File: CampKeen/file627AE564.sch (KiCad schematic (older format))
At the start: 16 parts, among them Q16 2N7000, Q17 2N7000, Q18 2N7000, Q19 2N7000

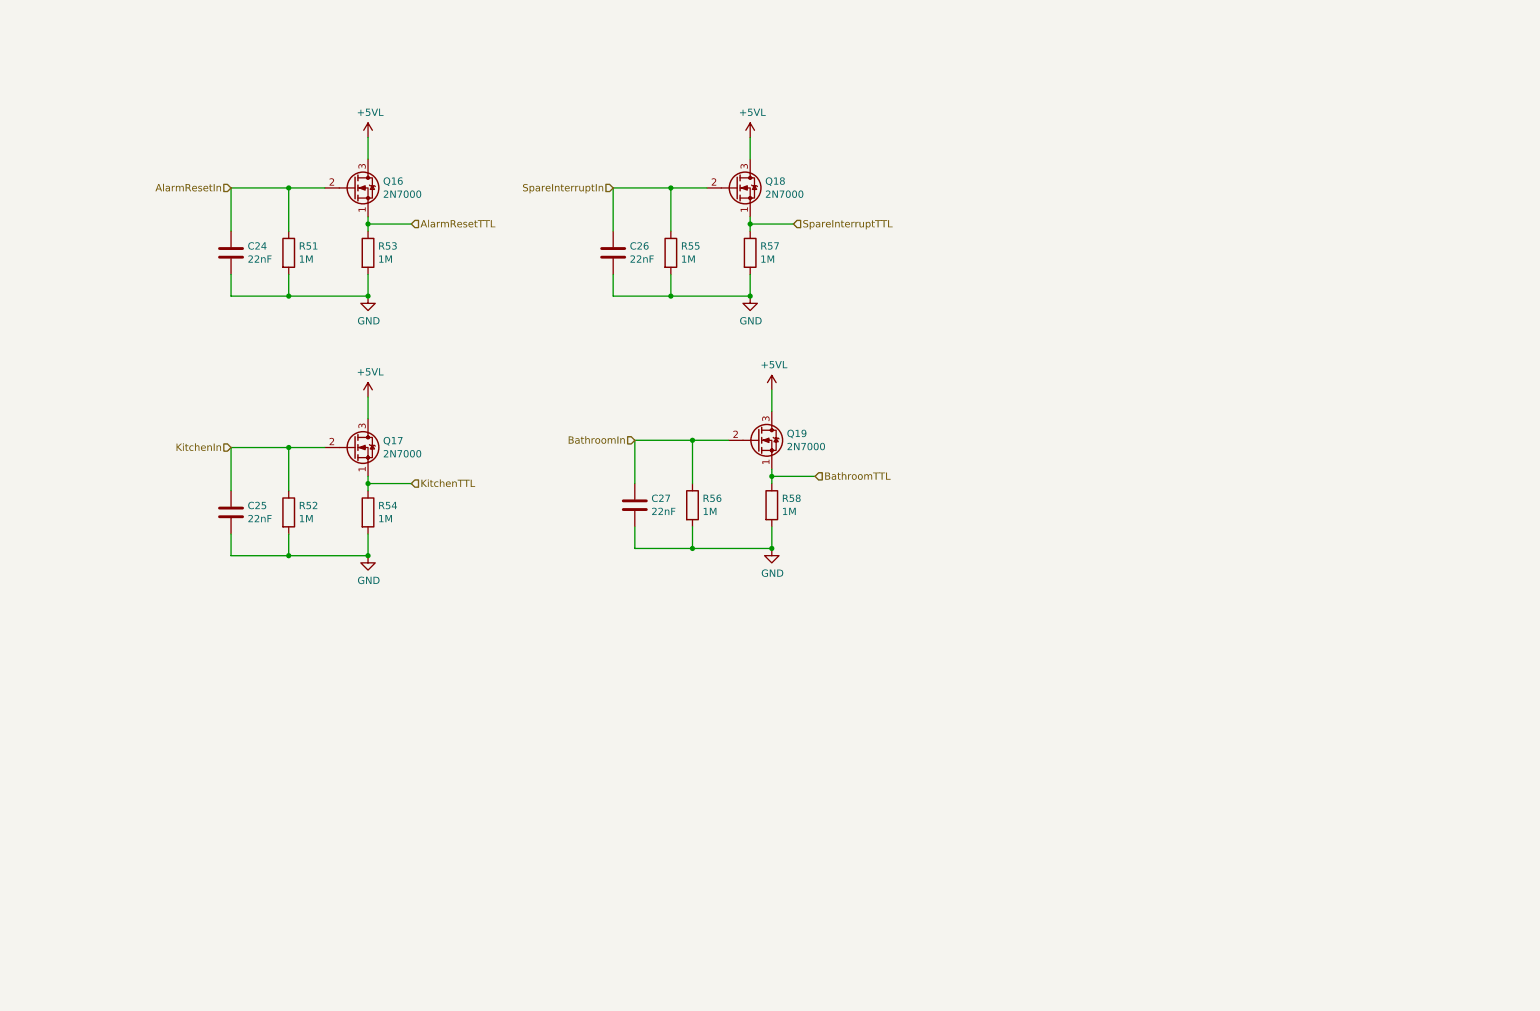
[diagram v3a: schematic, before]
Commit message: wip for working on the input circuits on the board. they are getting upgraded with opto-isolation as i've found that you can burn out the processor board if there is a voltage applied to an input when the system is on and then turned off. for the code fixing some of the LCD display code.
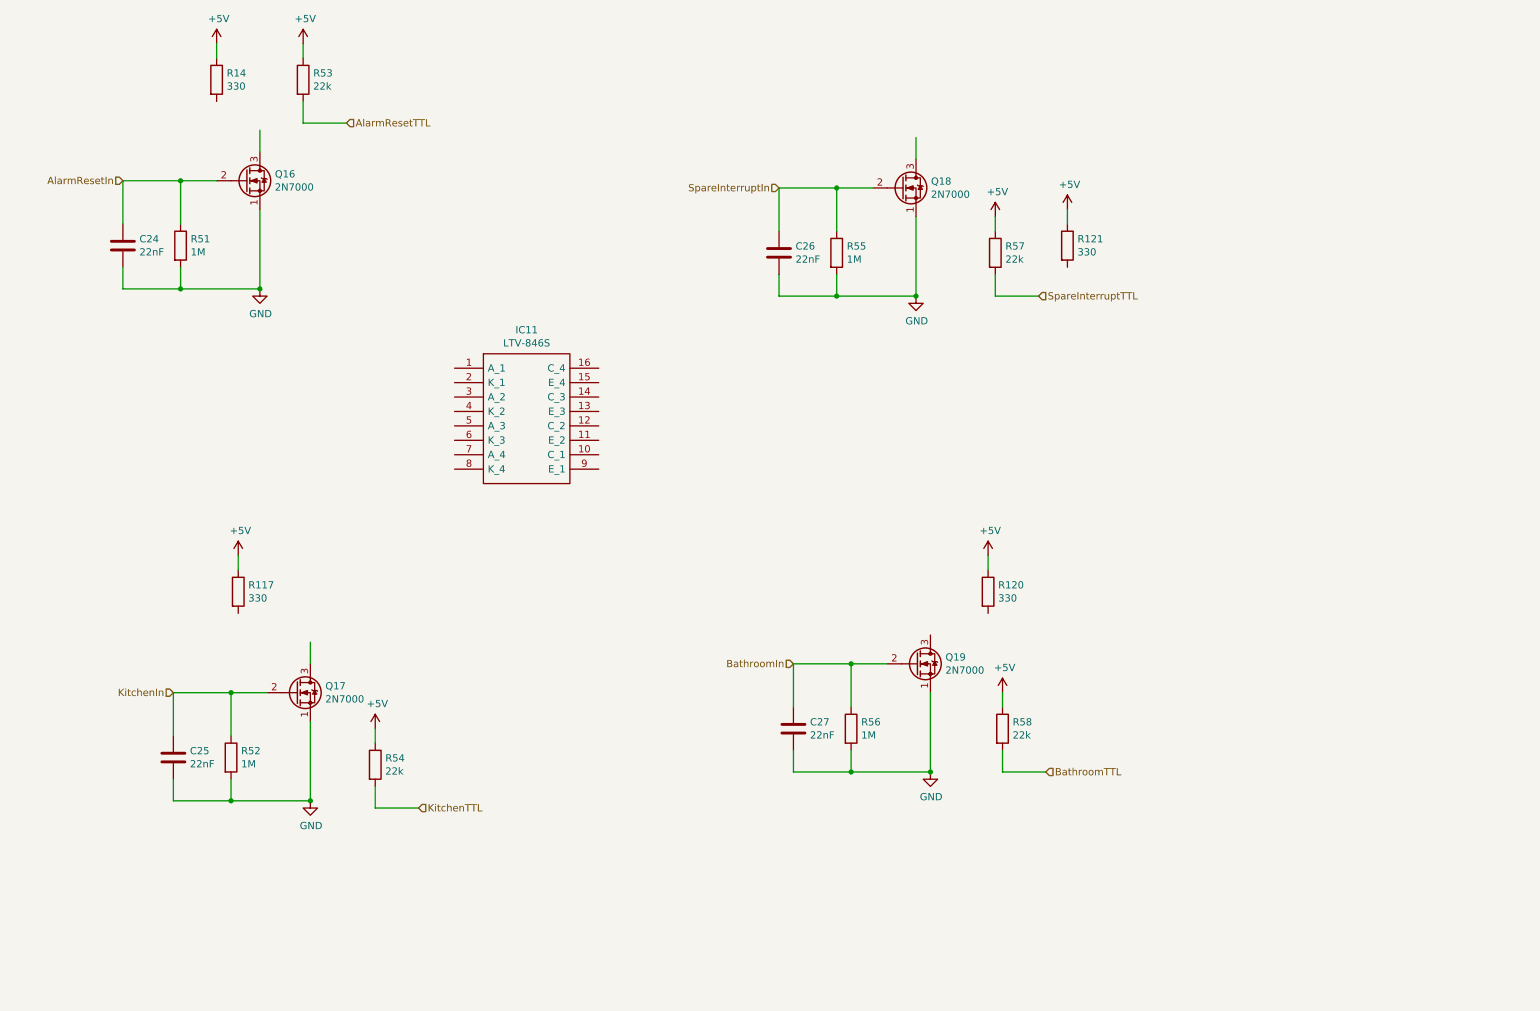
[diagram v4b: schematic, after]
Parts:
- added IC11: LTV-846S, SOP254P1016X460-16N, symbol SamacSys_Parts:LTV-846S
- added R117, R120, R121, R14: 330, Resistor_THT:R_Axial_DIN0207_L6.3mm_D2.5mm_P2.54mm_Vertical, symbol Device:R
- R53, R54, R57, R58: value 1M -> 22k
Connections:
- net labels added: +5V
- net labels removed: +5VL
- wire segments 52 -> 55
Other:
- moved on the sheet: C24, C25, C26, C27, Q16, Q17, Q18, Q19, R51, R52, R53, R54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

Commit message: schematic done for Input isolation updates.
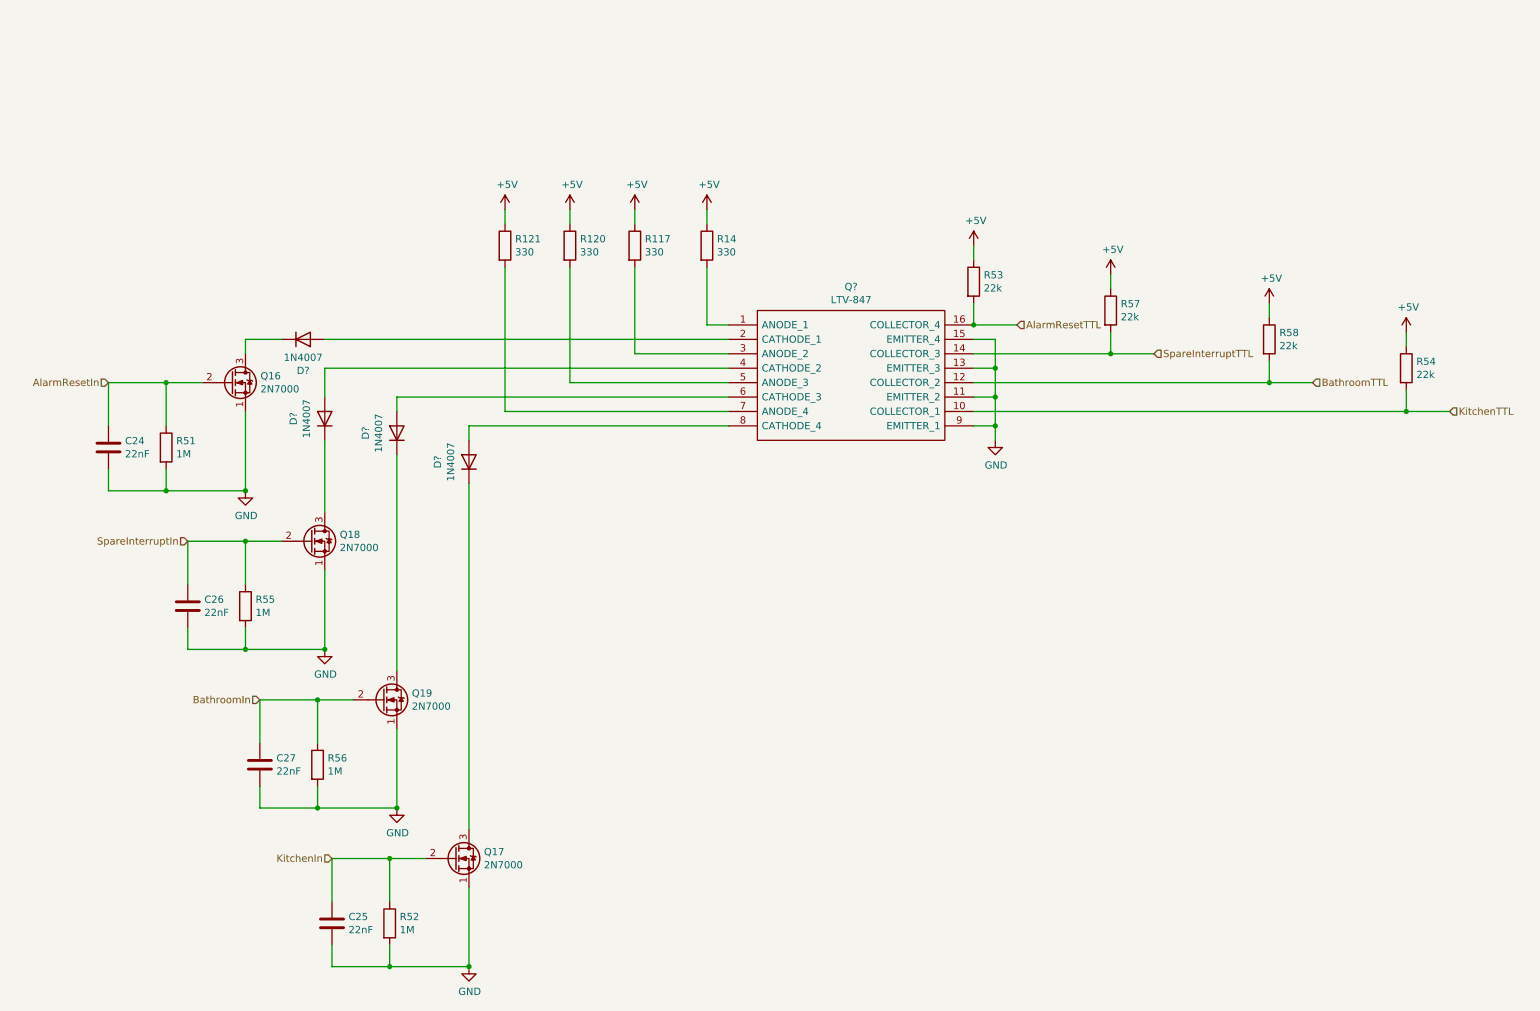
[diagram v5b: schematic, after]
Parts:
- removed IC11: LTV-846S, SOP254P1016X460-16N, symbol SamacSys_Parts:LTV-846S
- added D? (x4): 1N4007, Diode_THT:D_DO-41_SOD81_P10.16mm_Horizontal, symbol Diode:1N4007
- added Q?: LTV-847, DIP762W60P254L1984H450Q16N, symbol SamacSys_Parts:LTV-847
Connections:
- wire segments 55 -> 83
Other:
- moved on the sheet: C24, C25, C26, C27, Q16, Q17, Q18, Q19, R117, R120, R121, R14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

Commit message: added the appropriate power flags to the voltage rails as to make DRC Happy.
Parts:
- gave numbers to parts that had none: 5
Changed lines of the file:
@@
 $EndComp
 $Comp
-L SamacSys_Parts:LTV-847 Q?
+L SamacSys_Parts:LTV-847 Q60
 U 1 1 61CC4462
 P 5400 2800
-F 0 "Q?" H 6250 3065 50  0000 C CNN
+F 0 "Q60" H 6250 3065 50  0000 C CNN
 F 1 "LTV-847" H 6250 2974 50  0000 C CNN
 F 2 "DIP762W60P254L1984H450Q16N" H 6950 2900 50  0001 L CNN
@@
 AR Path="/6479D118/61CF45AE" Ref="D?"  Part="1"
 AR Path="/619922D7/61CF45AE" Ref="D?"  Part="1"
-AR Path="/627AE565/61CF45AE" Ref="D?"  Part="1"
-F 0 "D?" H 2600 3667 50  0000 C CNN
+AR Path="/627AE565/61CF45AE" Ref="D14"  Part="1"
+F 0 "D14" H 2600 3667 50  0000 C CNN
 F 1 "1N4007" H 2600 3576 50  0000 C CNN
 F 2 "Diode_THT:D_DO-41_SOD81_P10.16mm_Horizontal" H 2600 3275 50  0001 C CNN
@@
 AR Path="/6479D118/61CF45BA" Ref="D?"  Part="1"
 AR Path="/619922D7/61CF45BA" Ref="D?"  Part="1"
-AR Path="/627AE565/61CF45BA" Ref="D?"  Part="1"
-F 0 "D?" H 3600 3967 50  0000 C CNN
+AR Path="/627AE565/61CF45BA" Ref="D16"  Part="1"
+F 0 "D16" H 3600 3967 50  0000 C CNN
 F 1 "1N4007" H 3600 3876 50  0000 C CNN
 F 2 "Diode_THT:D_DO-41_SOD81_P10.16mm_Horizontal" H 3600 3575 50  0001 C CNN
@@
 AR Path="/6479D118/61CF45C0" Ref="D?"  Part="1"
 AR Path="/619922D7/61CF45C0" Ref="D?"  Part="1"
-AR Path="/627AE565/61CF45C0" Ref="D?"  Part="1"
-F 0 "D?" H 2450 3117 50  0000 C CNN
+AR Path="/627AE565/61CF45C0" Ref="D13"  Part="1"
+F 0 "D13" H 2450 3117 50  0000 C CNN
 F 1 "1N4007" H 2450 3026 50  0000 C CNN
 F 2 "Diode_THT:D_DO-41_SOD81_P10.16mm_Horizontal" H 2450 2725 50  0001 C CNN
@@
 AR Path="/62665296/61D587EB" Ref="#PWR?"  Part="1"
 AR Path="/6479D118/61D587EB" Ref="#PWR?"  Part="1"
-AR Path="/627AE565/61D587EB" Ref="#PWR?"  Part="1"
-F 0 "#PWR?" H 7250 3350 50  0001 C CNN
+AR Path="/627AE565/61D587EB" Ref="#PWR0164"  Part="1"
+F 0 "#PWR0164" H 7250 3350 50  0001 C CNN
 F 1 "GND" H 7255 3427 50  0000 C CNN
 F 2 "" H 7250 3600 50  0001 C CNN
@@
 AR Path="/6479D118/61CF45B4" Ref="D?"  Part="1"
 AR Path="/619922D7/61CF45B4" Ref="D?"  Part="1"
-AR Path="/627AE565/61CF45B4" Ref="D?"  Part="1"
-F 0 "D?" H 3100 3767 50  0000 C CNN
+AR Path="/627AE565/61CF45B4" Ref="D15"  Part="1"
+F 0 "D15" H 3100 3767 50  0000 C CNN
 F 1 "1N4007" H 3100 3676 50  0000 C CNN
 F 2 "Diode_THT:D_DO-41_SOD81_P10.16mm_Horizontal" H 3100 3375 50  0001 C CNN
